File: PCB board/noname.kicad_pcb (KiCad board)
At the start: 2 copper layers, 58.2 x 27.9 mm, 14 parts

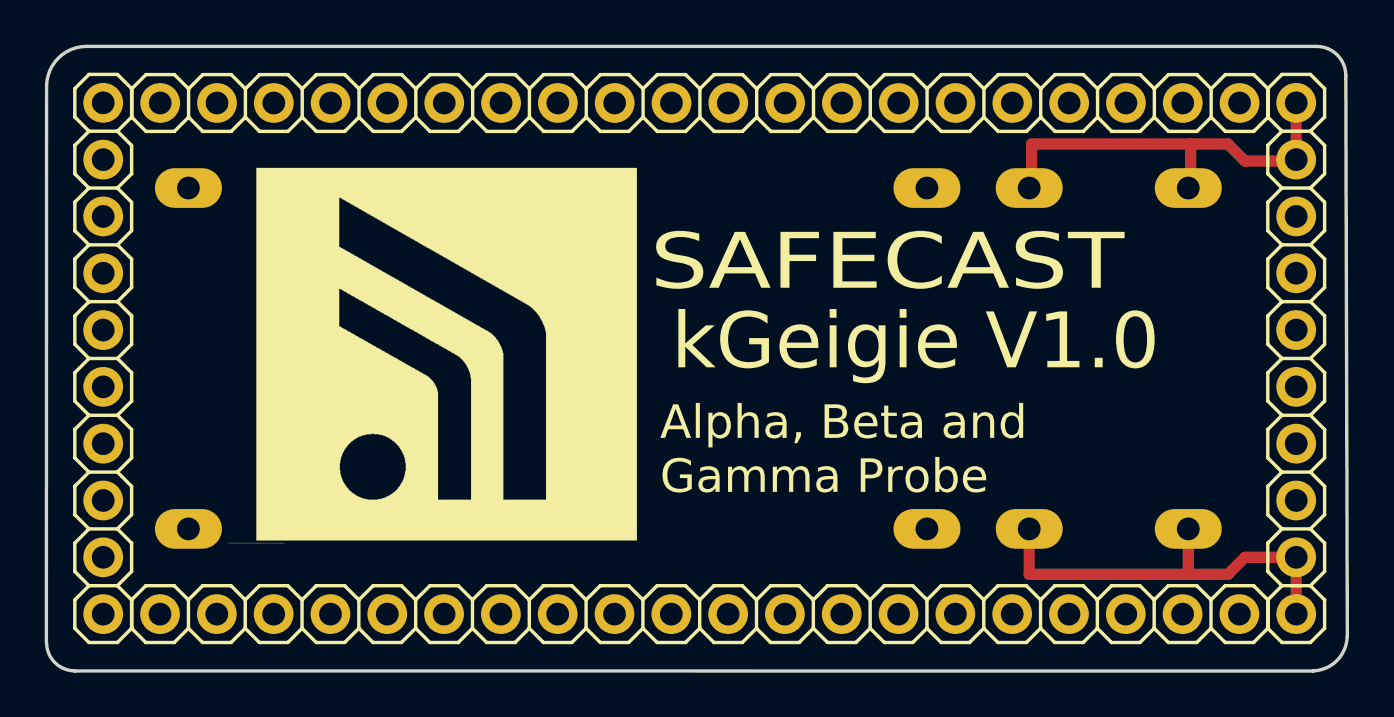
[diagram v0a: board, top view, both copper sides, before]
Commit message: Added schema setup for M5Stack hookup
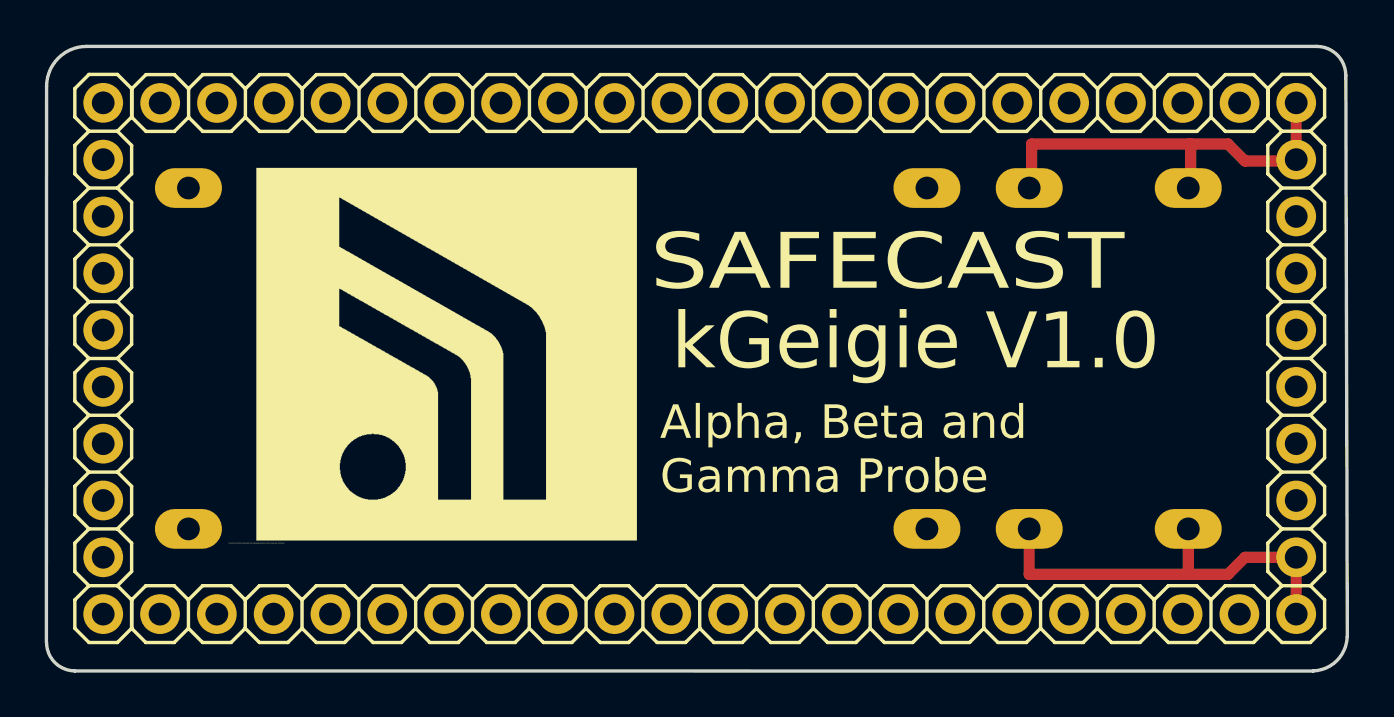
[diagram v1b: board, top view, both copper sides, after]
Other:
- net class Default removed
